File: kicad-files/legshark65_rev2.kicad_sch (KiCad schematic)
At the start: 201 parts, among them J1 ARM JTAG, SW1 K2-1187SQ-A4SW-06, SW2 PCM12SMTR, T2 53261-0471, U1 STM32F411CEU6, U2 MCP1700T-3302E/TT, U3 AT24C256C-SSHL-T, Y1 TAXM8M4RFDCET2T

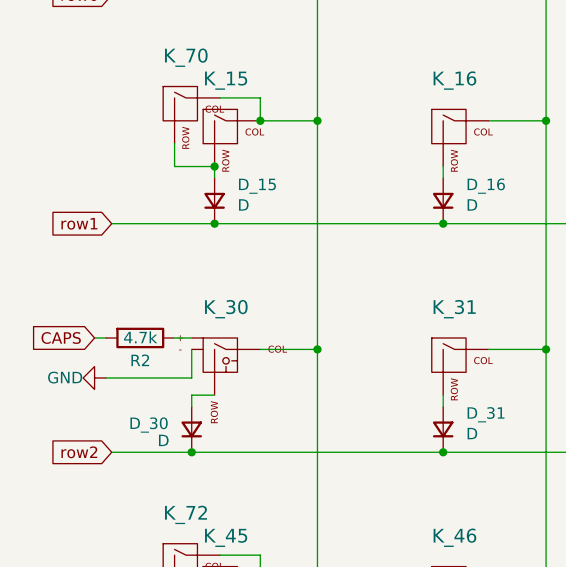
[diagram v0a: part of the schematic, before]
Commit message: Added some more comments to schematic
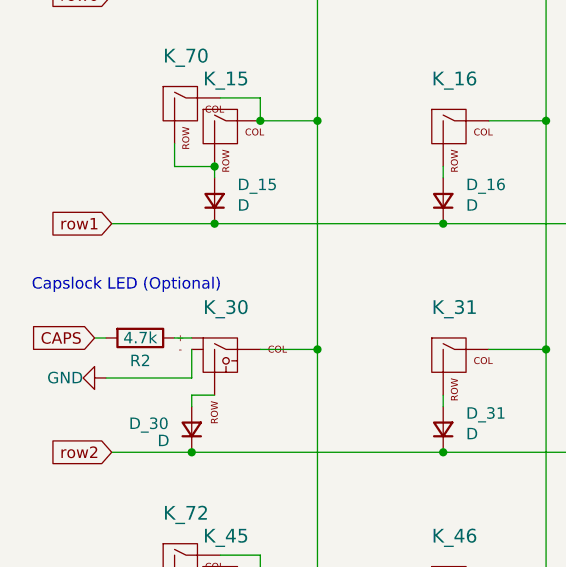
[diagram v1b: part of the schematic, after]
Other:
- note added: "Capslock LED (Optional)"
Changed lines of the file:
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@@
     (effects (font (size 3 3) (thickness 0.6) bold) (justify right bottom))
+  )
+  (text "Capslock LED (Optional)" (at 13.97 68.58 0)
+    (effects (font (size 1.27 1.27)) (justify left bottom))
   )
   (text "Leave R5 unpopulated as per specs for MCU" (at 236.855 224.155 0)

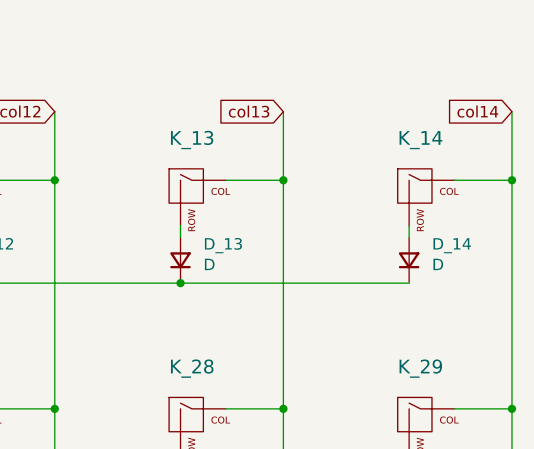
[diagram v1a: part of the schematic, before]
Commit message: Added 2u key option instead of DEL
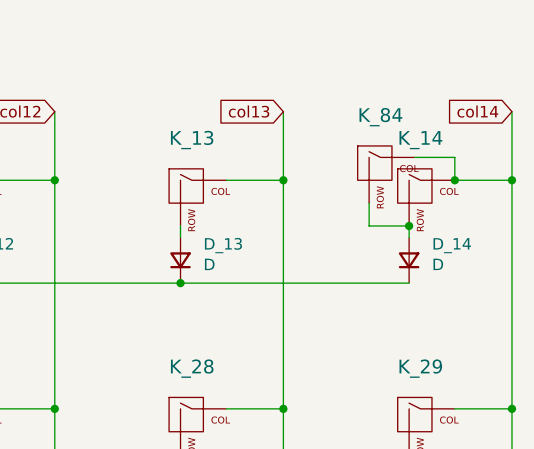
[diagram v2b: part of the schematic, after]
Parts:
- added K_84: KEYSW, MX_Only:MXOnly-2U-NoLED, symbol MX_Alps_Hybrid:MX-NoLED
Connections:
- net col14: now also K_84.1 (COL)
- net at D_14.2 (A), K_14.2 (ROW): now also K_84.2 (ROW)
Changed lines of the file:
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@@
   (junction (at 262.89 86.36) (diameter 0) (color 0 0 0 0)
   )
+  (junction (at 389.89 29.21) (diameter 0) (color 0 0 0 0)
+  )
   (junction (at 350.52 49.53) (diameter 0) (color 0 0 0 0)
   )
@@
   (junction (at 64.77 125.73) (diameter 0) (color 0 0 0 0)
   )
+  (junction (at 394.97 24.13) (diameter 0) (color 0 0 0 0)
+  )
   (junction (at 186.69 111.76) (diameter 0) (color 0 0 0 0)
   )
@@
     (stroke (width 0) (type default))
   )
+  (wire (pts (xy 385.445 26.67) (xy 385.445 29.21))
+    (stroke (width 0) (type default))
+  )
   (wire (pts (xy 90.17 24.13) (xy 96.52 24.13))
     (stroke (width 0) (type default))
@@
     (stroke (width 0) (type default))
   )
+  (wire (pts (xy 390.525 21.59) (xy 394.97 21.59))
+    (stroke (width 0) (type default))
+  )
   (wire (pts (xy 262.89 54.61) (xy 262.89 55.88))
     (stroke (width 0) (type default))
@@
     (stroke (width 0) (type default))
   )
+  (wire (pts (xy 385.445 29.21) (xy 389.89 29.21))
+    (stroke (width 0) (type default))
+  )
   (wire (pts (xy 107.95 180.34) (xy 114.3 180.34))
     (stroke (width 0) (type default))
@@
     (stroke (width 0) (type default))
   )
+  (wire (pts (xy 394.97 21.59) (xy 394.97 24.13))
+    (stroke (width 0) (type default))
+  )
   (wire (pts (xy 262.89 35.56) (xy 288.29 35.56))
     (stroke (width 0) (type default))
@@
         )
       )
+    )
+  )
+  (symbol (lib_id "MX_Alps_Hybrid:MX-NoLED") (at 386.715 22.86 0) (unit 1)
+    (in_bom yes) (on_board yes) (dnp no)
+    (property "Reference" "K_84" (at 386.715 16.9418 0)
+      (effects (font (size 1.524 1.524)))
+    )
+    (property "Value" "KEYSW" (at 386.715 25.4 0)
+      (effects (font (size 1.524 1.524)) hide)
+    )
+    (property "Footprint" "MX_Only:MXOnly-2U-NoLED" (at 386.715 22.86 0)
+      (effects (font (size 1.524 1.524)) hide)
+    )
+    (property "Datasheet" "" (at 386.715 22.86 0)
+      (effects (font (size 1.524 1.524)))
+    )
+    (pin "1")
+    (pin "2")
+    (instances
+      (project "legshark65_rev2"
+        (path "/2fcc1073-d3f4-43f9-b3b4-5cee13272705"
+          (reference "K_84") (unit 1)
+        )
+      )

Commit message: Updating board graphics
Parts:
- removed H2: FrontSilk, Legshark:Legshark_Logo_Huge, symbol Mechanical:MountingHole
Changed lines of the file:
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@@
-    )
-  )
-  (symbol (lib_id "Mechanical:MountingHole") (at 244.475 187.96 0) (unit 1)
-    (in_bom yes) (on_board yes) (dnp no) (fields_autoplaced)
-    (property "Reference" "H2" (at 247.015 187.325 0)
-      (effects (font (size 1.27 1.27)) (justify left))
-    )
-    (property "Value" "FrontSilk" (at 247.015 189.865 0)
-      (effects (font (size 1.27 1.27)) (justify left))
-    )
-    (property "Footprint" "Legshark:Legshark_Logo_Huge" (at 244.475 187.96 0)
-      (effects (font (size 1.27 1.27)) hide)
-    )
-    (property "Datasheet" "~" (at 244.475 187.96 0)
-      (effects (font (size 1.27 1.27)) hide)
-    )
-    (instances
-      (project "legshark65_rev2"
-        (path "/2fcc1073-d3f4-43f9-b3b4-5cee13272705"
-          (reference "H2") (unit 1)
-        )
-      )
-      (project "legshark65_rev1"
-        (path "/9ddf6dc5-8b5e-413a-9b25-d1d5a5a60469"
-          (reference "H3") (unit 1)
-        )
-      )
     )
   )

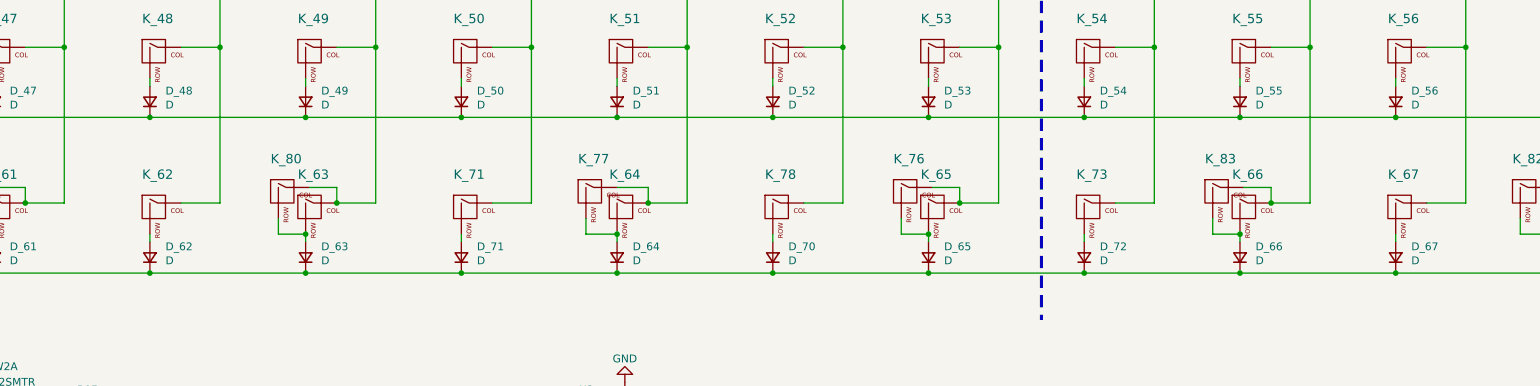
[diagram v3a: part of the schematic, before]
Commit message: Added extra 1.5 and cut out the corners
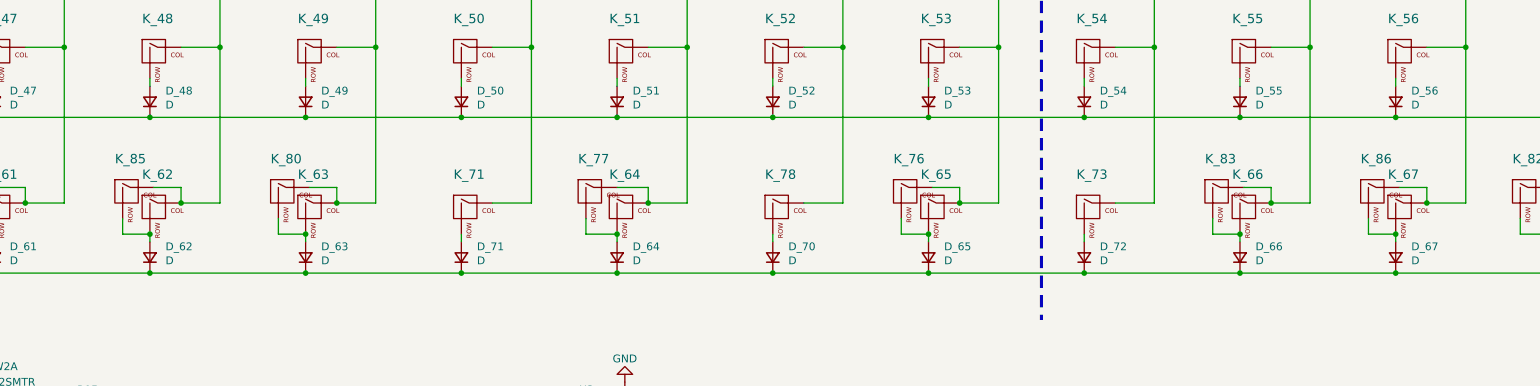
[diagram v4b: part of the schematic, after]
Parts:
- added K_85, K_86: KEYSW, MX_Only:MXOnly-1.5U-NoLED, symbol MX_Alps_Hybrid:MX-NoLED
- K_72: footprint MX_Only:MXOnly-2U-NoLED -> MX_Only:MXOnly-2U-ReversedStabilizers-NoLED
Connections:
- net col11: now also K_86.1 (COL)
- net col3: now also K_85.1 (COL)
- net at D_67.2 (A), K_67.2 (ROW): now also K_86.2 (ROW)
- net at D_62.2 (A), K_62.2 (ROW): now also K_85.2 (ROW)
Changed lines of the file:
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@@
 (kicad_sch (version 20230121) (generator eeschema)
   (paper "A2")
+  (junction (at 115.57 125.73) (diameter 0) (color 0 0 0 0)
+  )
   (junction (at 85.09 35.56) (diameter 0) (color 0 0 0 0)
   )
@@
   (junction (at 237.49 130.81) (diameter 0) (color 0 0 0 0)
   )
+  (junction (at 318.77 125.73) (diameter 0) (color 0 0 0 0)
+  )
   (junction (at 59.69 137.16) (diameter 0) (color 0 0 0 0)
   )
@@
   (junction (at 262.89 111.76) (diameter 0) (color 0 0 0 0)
   )
+  (junction (at 110.49 130.81) (diameter 0) (color 0 0 0 0)
+  )
   (junction (at 325.12 24.13) (diameter 0) (color 0 0 0 0)
   )
@@
   (junction (at 313.69 111.76) (diameter 0) (color 0 0 0 0)
   )
+  (junction (at 313.69 130.81) (diameter 0) (color 0 0 0 0)
+  )
   (junction (at 198.12 100.33) (diameter 0) (color 0 0 0 0)
   )
@@
     (stroke (width 0) (type default))
   )
+  (wire (pts (xy 309.245 128.27) (xy 309.245 130.81))
+    (stroke (width 0) (type default))
+  )
   (wire (pts (xy 140.97 24.13) (xy 147.32 24.13))
     (stroke (width 0) (type default))
@@
     (stroke (width 0) (type default))
   )
+  (wire (pts (xy 106.045 130.81) (xy 110.49 130.81))
+    (stroke (width 0) (type default))
+  )
   (wire (pts (xy 90.17 24.13) (xy 96.52 24.13))
     (stroke (width 0) (type default))
   )
+  (wire (pts (xy 106.045 128.27) (xy 106.045 130.81))
+    (stroke (width 0) (type default))
+  )
   (wire (pts (xy 140.97 74.93) (xy 147.32 74.93))
     (stroke (width 0) (type default))
@@
     (stroke (width 0) (type default))
   )
+  (wire (pts (xy 309.245 130.81) (xy 313.69 130.81))
+    (stroke (width 0) (type default))
+  )
   (wire (pts (xy 172.72 74.93) (xy 172.72 49.53))
     (stroke (width 0) (type default))
@@
     (stroke (width 0) (type default))
   )
+  (wire (pts (xy 318.77 123.19) (xy 318.77 125.73))
+    (stroke (width 0) (type default))
+  )
   (wire (pts (xy 369.57 123.19) (xy 369.57 125.73))
     (stroke (width 0) (type default))
@@
     (stroke (width 0) (type default))
   )
+  (wire (pts (xy 111.125 123.19) (xy 115.57 123.19))
+    (stroke (width 0) (type default))
+  )
   (wire (pts (xy 59.69 130.81) (xy 59.69 132.08))
     (stroke (width 0) (type default))
@@
     (stroke (width 0) (type default))
   )
+  (wire (pts (xy 115.57 123.19) (xy 115.57 125.73))
+    (stroke (width 0) (type default))
+  )
   (wire (pts (xy 34.29 35.56) (xy 59.69 35.56))
     (stroke (width 0) (type default))
@@
     (stroke (width 0) (type default))
   )
+  (wire (pts (xy 314.325 123.19) (xy 318.77 123.19))
+    (stroke (width 0) (type default))
+  )
   (wire (pts (xy 64.77 49.53) (xy 71.12 49.53))
     (stroke (width 0) (type default))
@@
       (effects (font (size 1.524 1.524)) hide)
     )
-    (property "Footprint" "MX_Only:MXOnly-2U-NoLED" (at 31.115 99.06 0)
+    (property "Footprint" "MX_Only:MXOnly-2U-ReversedStabilizers-NoLED" (at 31.115 99.06 0)
       (effects (font (size 1.524 1.524)) hide)
     )
@@
     )
   )
+  (symbol (lib_id "MX_Alps_Hybrid:MX-NoLED") (at 107.315 124.46 0) (unit 1)
+    (in_bom yes) (on_board yes) (dnp no)
+    (property "Reference" "K_85" (at 107.315 118.5418 0)
+      (effects (font (size 1.524 1.524)))
+    )
+    (property "Value" "KEYSW" (at 107.315 127 0)
+      (effects (font (size 1.524 1.524)) hide)
+    )
+    (property "Footprint" "MX_Only:MXOnly-1.5U-NoLED" (at 107.315 124.46 0)
+      (effects (font (size 1.524 1.524)) hide)
+    )
+    (property "Datasheet" "" (at 107.315 124.46 0)
+      (effects (font (size 1.524 1.524)))
+    )
+    (pin "1")
+    (pin "2")
+    (instances
+      (project "legshark65_rev2"
+        (path "/2fcc1073-d3f4-43f9-b3b4-5cee13272705"
+          (reference "K_85") (unit 1)
+        )
+      )
+    )
+  )
   (symbol (lib_name "MountingHole_4") (lib_id "Mechanical:MountingHole") (at 285.75 185.42 0) (unit 1)
     (in_bom yes) (on_board yes) (dnp no) (fields_autoplaced)
@@
         )
       )
+    )
+  )
+  (symbol (lib_id "MX_Alps_Hybrid:MX-NoLED") (at 310.515 124.46 0) (unit 1)
+    (in_bom yes) (on_board yes) (dnp no)
+    (property "Reference" "K_86" (at 310.515 118.5418 0)
+      (effects (font (size 1.524 1.524)))
+    )
+    (property "Value" "KEYSW" (at 310.515 127 0)
+      (effects (font (size 1.524 1.524)) hide)
+    )
+    (property "Footprint" "MX_Only:MXOnly-1.5U-NoLED" (at 310.515 124.46 0)
+      (effects (font (size 1.524 1.524)) hide)
+    )
+    (property "Datasheet" "" (at 310.515 124.46 0)
+      (effects (font (size 1.524 1.524)))
+    )
+    (pin "1")
+    (pin "2")
+    (instances
+      (project "legshark65_rev2"
+        (path "/2fcc1073-d3f4-43f9-b3b4-5cee13272705"
+          (reference "K_86") (unit 1)
+        )
+      )
